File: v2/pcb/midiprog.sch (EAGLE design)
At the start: 56 parts, among them IC1 PIC18F4550_40, IC2 TPIC6B596N, IC4 TPIC6B596N, Q2 2N2222A, Q3 2N2222A, Q4 2N2222A, Q5 8MHz

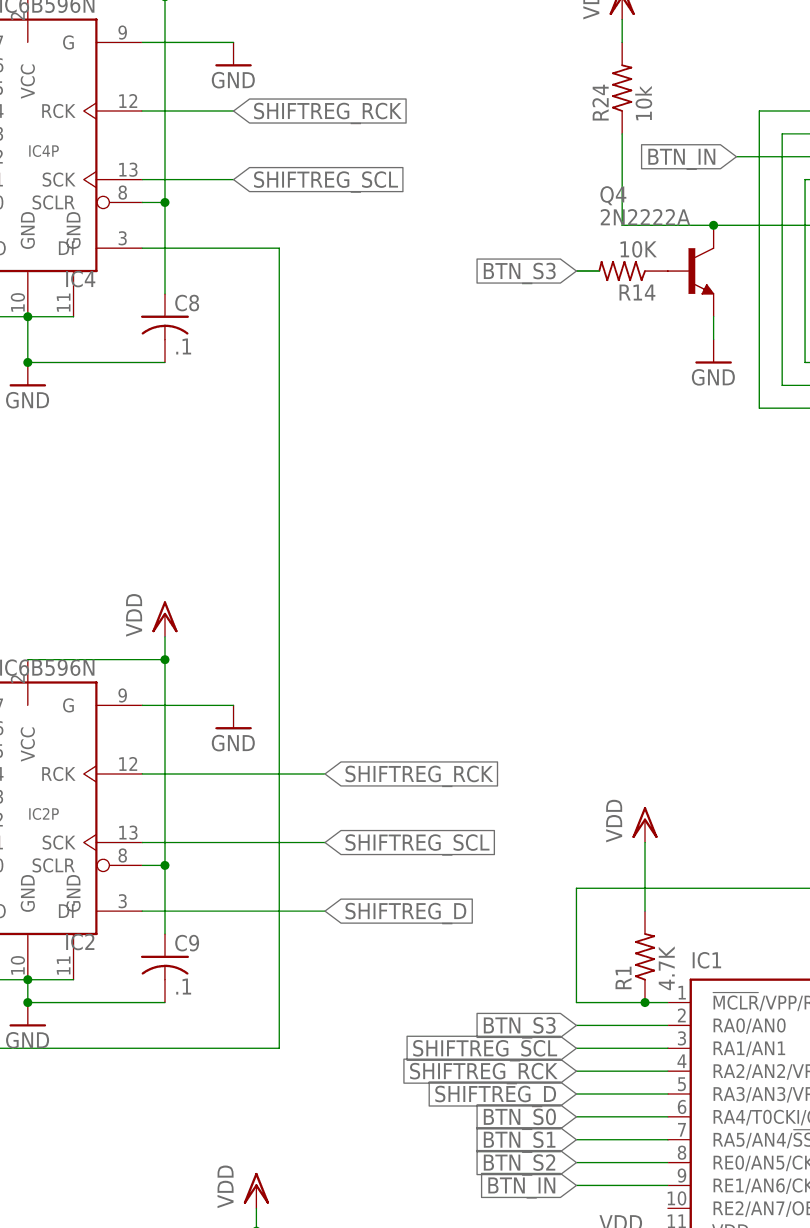
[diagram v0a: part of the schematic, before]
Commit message: Named connections better on schematic.
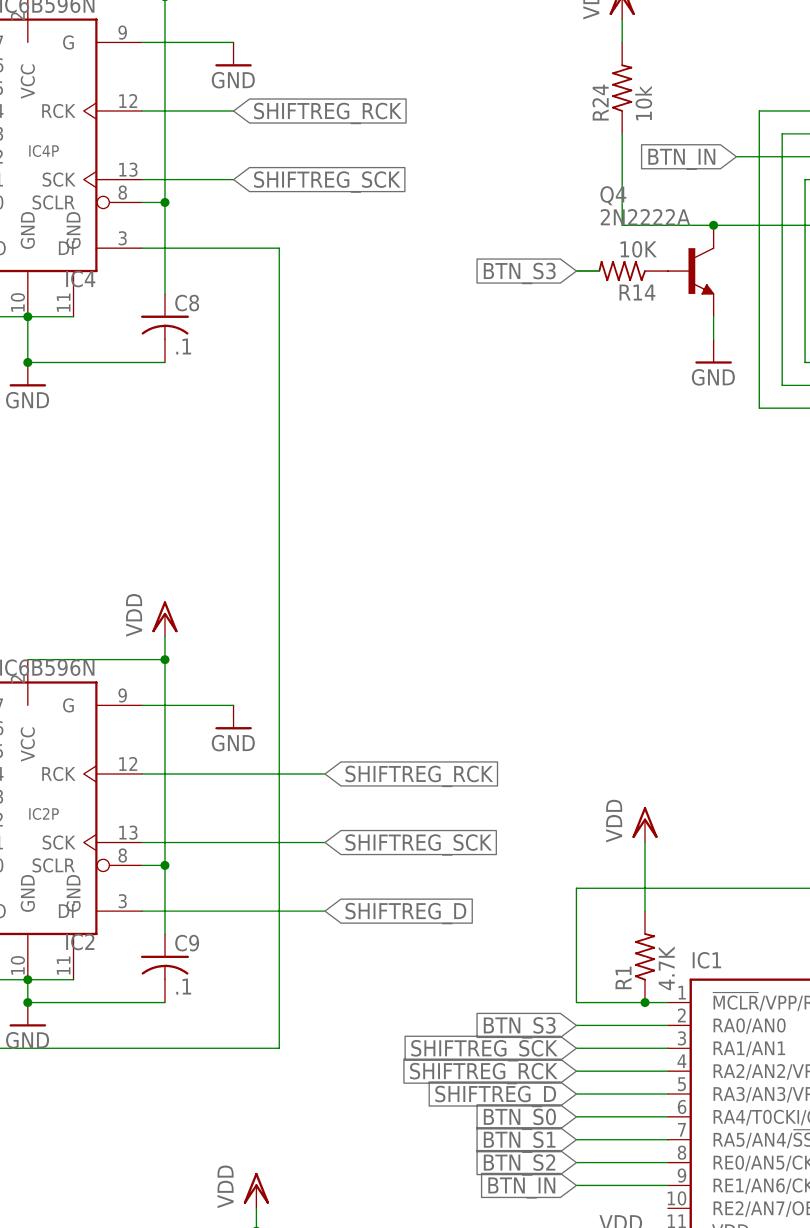
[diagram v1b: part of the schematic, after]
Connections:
- net N$46 renamed BTN_TOP_6
- net N$47 renamed BTN_BOT_6
- net N$48 renamed BTN_TOP_8
- net N$49 renamed BTN_TOP_7
- net N$50 renamed BTN_BOT_8
- net N$51 renamed BTN_BOT_7
- net N$52 renamed BTN_BOT_5
- net N$55 renamed BTN_BOT_4
- net N$56 renamed BTN_BOT_1
- net N$57 renamed BTN_BOT_2
- net N$58 renamed BTN_BOT_3
- net N$60 renamed BTN_TOP_5
- net N$61 renamed BTN_TOP_4
- net N$62 renamed BTN_TOP_1
- net N$63 renamed BTN_TOP_2
- net N$64 renamed BTN_TOP_3
- net SHIFTREG_SCL renamed SHIFTREG_SCK
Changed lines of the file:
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@@
 </segment>
 </net>
-<net name="SHIFTREG_SCL" class="0">
+<net name="SHIFTREG_SCK" class="0">
 <segment>
 <wire x1="193.04" y1="60.96" x2="213.36" y2="60.96" width="0.1524" layer="91"/>
@@
 </segment>
 </net>
-<net name="N$46" class="0">
+<net name="BTN_TOP_6" class="0">
 <segment>
 <pinref part="U$2" gate="G$1" pin="A5"/>
@@
 </segment>
 </net>
-<net name="N$48" class="0">
+<net name="BTN_TOP_8" class="0">
 <segment>
 <pinref part="U$2" gate="G$1" pin="A7"/>
@@
 </segment>
 </net>
-<net name="N$49" class="0">
+<net name="BTN_TOP_7" class="0">
 <segment>
 <pinref part="BTN_FX_CN" gate="G$1" pin="13"/>
@@
 </segment>
 </net>
-<net name="N$60" class="0">
+<net name="BTN_TOP_5" class="0">
 <segment>
 <pinref part="BTN_FX_CN" gate="G$1" pin="15"/>
@@
 </segment>
 </net>
-<net name="N$61" class="0">
+<net name="BTN_TOP_4" class="0">
 <segment>
 <pinref part="BTN_FX_CN" gate="G$1" pin="7"/>
@@
 </segment>
 </net>
-<net name="N$62" class="0">
+<net name="BTN_TOP_1" class="0">
 <segment>
 <pinref part="BTN_FX_CN" gate="G$1" pin="5"/>
@@
 </segment>
 </net>
-<net name="N$63" class="0">
+<net name="BTN_TOP_2" class="0">
 <segment>
 <pinref part="BTN_FX_CN" gate="G$1" pin="3"/>
@@
 </segment>
 </net>
-<net name="N$64" class="0">
+<net name="BTN_TOP_3" class="0">
 <segment>
 <pinref part="BTN_FX_CN" gate="G$1" pin="1"/>
@@
 </segment>
 </net>
-<net name="N$47" class="0">
+<net name="BTN_BOT_6" class="0">
 <segment>
 <pinref part="BTN_PR_CN" gate="G$1" pin="9"/>
@@
 </segment>
 </net>
-<net name="N$50" class="0">
+<net name="BTN_BOT_8" class="0">
 <segment>
 <pinref part="BTN_PR_CN" gate="G$1" pin="11"/>
@@
 </segment>
 </net>
-<net name="N$51" class="0">
+<net name="BTN_BOT_7" class="0">
 <segment>
 <pinref part="BTN_PR_CN" gate="G$1" pin="13"/>
@@
 </segment>
 </net>
-<net name="N$52" class="0">
+<net name="BTN_BOT_5" class="0">
 <segment>
 <pinref part="BTN_PR_CN" gate="G$1" pin="15"/>
@@
 </segment>
 </net>
-<net name="N$55" class="0">
+<net name="BTN_BOT_4" class="0">
 <segment>
 <pinref part="BTN_PR_CN" gate="G$1" pin="7"/>
@@
 </segment>
 </net>
-<net name="N$56" class="0">
+<net name="BTN_BOT_1" class="0">
 <segment>
 <pinref part="BTN_PR_CN" gate="G$1" pin="5"/>
@@
 </segment>
 </net>
-<net name="N$57" class="0">
+<net name="BTN_BOT_2" class="0">
 <segment>
 <pinref part="BTN_PR_CN" gate="G$1" pin="3"/>
@@
 </segment>
 </net>
-<net name="N$58" class="0">
+<net name="BTN_BOT_3" class="0">
 <segment>
 <pinref part="BTN_PR_CN" gate="G$1" pin="1"/>

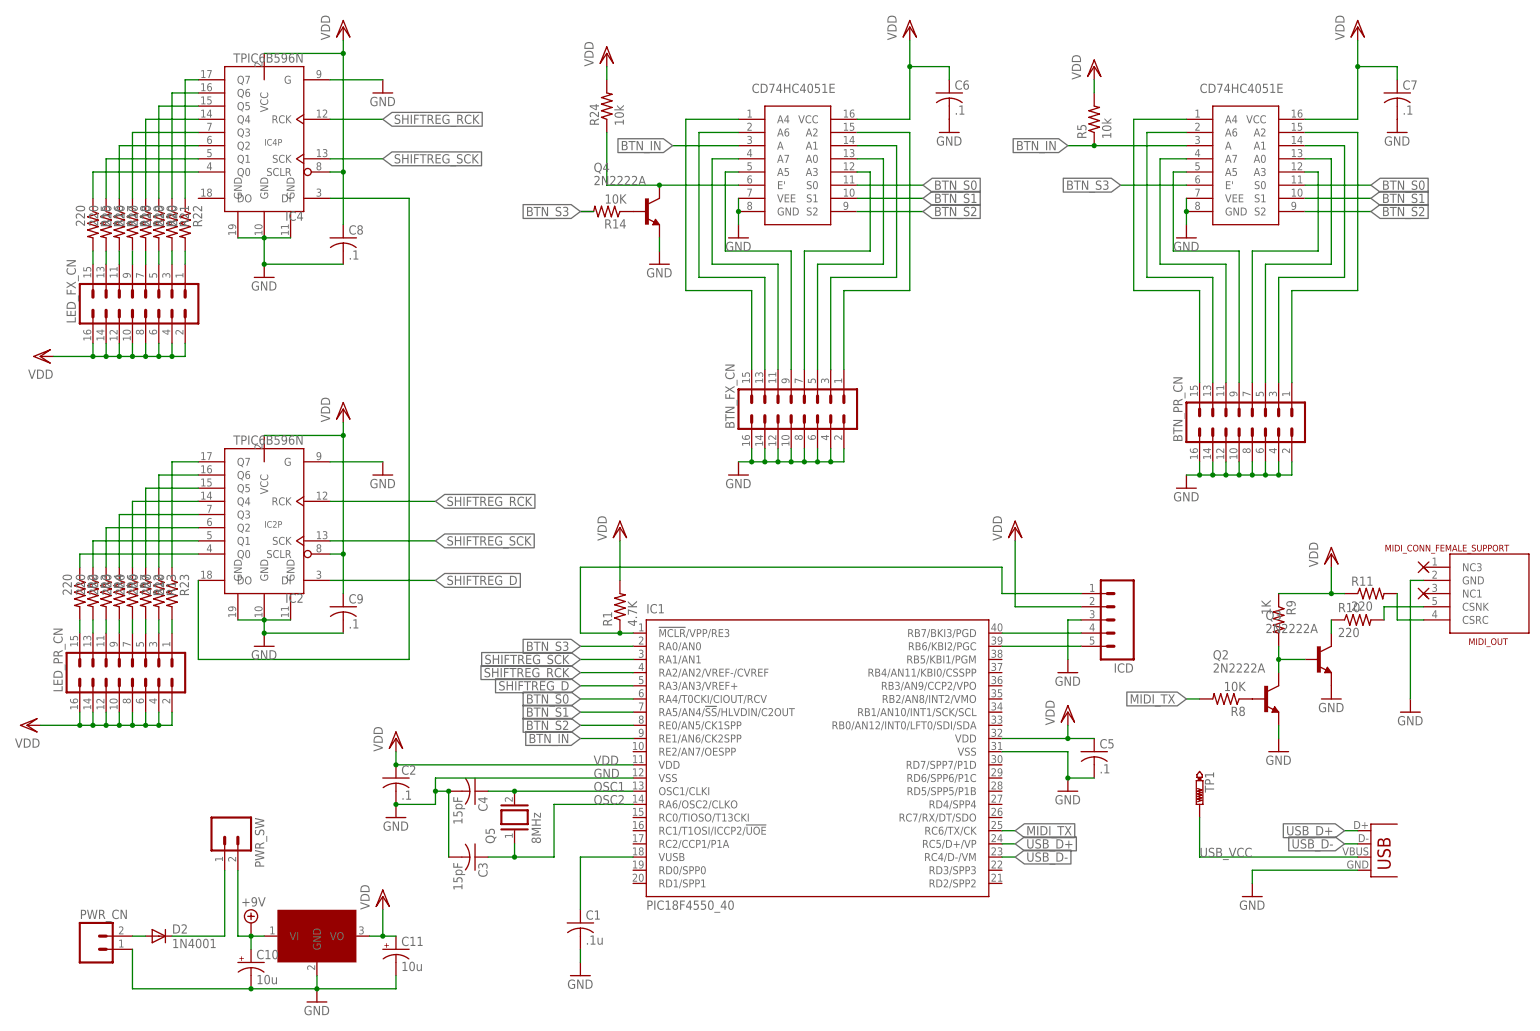
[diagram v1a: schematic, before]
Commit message: Renamed pins and connectors on schematic and added proper labels.
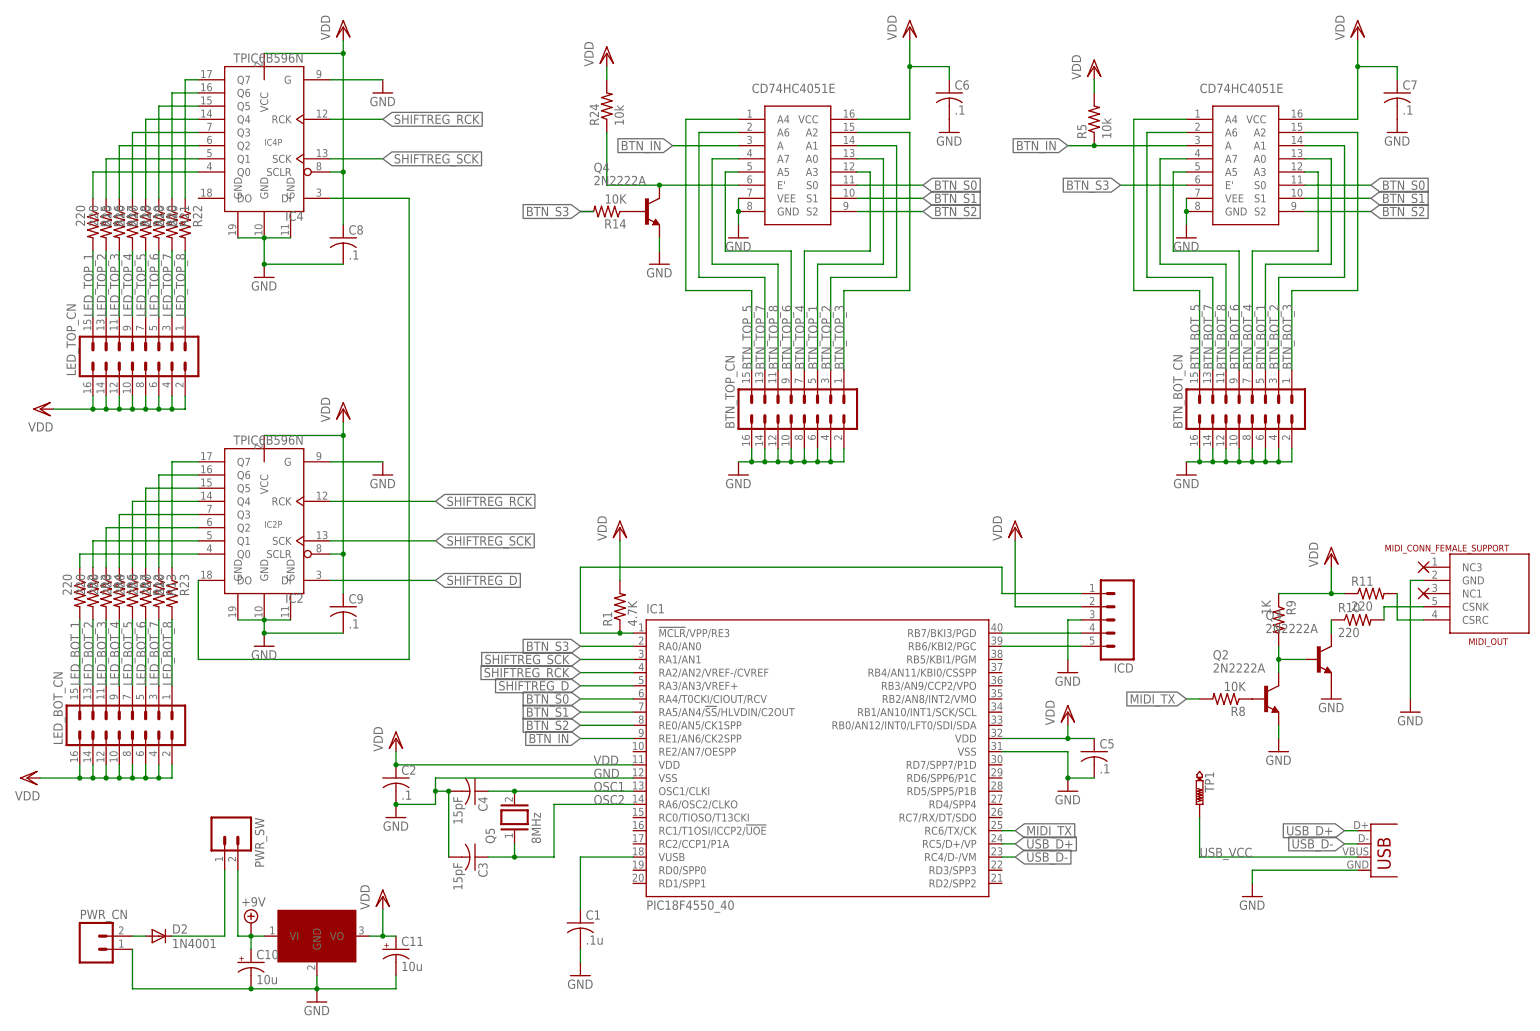
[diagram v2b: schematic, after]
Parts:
- removed BTN_PR_CN, LED_FX_CN, LED_PR_CN: (no value), con-lstb:MA08-2
- added BTN_BOT_CN, LED_BOT_CN, LED_TOP_CN: (no value), con-lstb:MA08-2
- renumbered BTN_FX_CN to BTN_TOP_CN
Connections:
- removed net N$10: LED_FX_CN.11, R17.2
- removed net N$11: LED_FX_CN.9, R18.2
- removed net N$12: LED_FX_CN.7, R19.2
- removed net N$13: LED_FX_CN.5, R20.2
- removed net N$14: LED_FX_CN.3, R21.2
- removed net N$15: LED_FX_CN.1, R22.2
- removed net N$2: LED_FX_CN.15, R15.2
- removed net N$24: LED_PR_CN.13, R3.2
- removed net N$27: LED_PR_CN.11, R4.2
- removed net N$28: LED_PR_CN.9, R6.2
- removed net N$3: LED_FX_CN.13, R16.2
- removed net N$30: LED_PR_CN.7, R7.2
- removed net N$32: LED_PR_CN.5, R12.2
- removed net N$36: LED_PR_CN.3, R13.2
- removed net N$37: LED_PR_CN.1, R23.2
- removed net N$6: LED_PR_CN.15, R2.2
- new net LED_BOT_1: LED_BOT_CN.15, R2.2
- new net LED_BOT_2: LED_BOT_CN.13, R3.2
- new net LED_BOT_3: LED_BOT_CN.11, R4.2
- new net LED_BOT_4: LED_BOT_CN.9, R6.2
- new net LED_BOT_5: LED_BOT_CN.7, R7.2
- new net LED_BOT_6: LED_BOT_CN.5, R12.2
- new net LED_BOT_7: LED_BOT_CN.3, R13.2
- new net LED_BOT_8: LED_BOT_CN.1, R23.2
- new net LED_TOP_1: LED_TOP_CN.15, R15.2
- new net LED_TOP_2: LED_TOP_CN.13, R16.2
- new net LED_TOP_3: LED_TOP_CN.11, R17.2
- new net LED_TOP_4: LED_TOP_CN.9, R18.2
- new net LED_TOP_5: LED_TOP_CN.7, R19.2
- new net LED_TOP_6: LED_TOP_CN.5, R20.2
- new net LED_TOP_7: LED_TOP_CN.3, R21.2
- new net LED_TOP_8: LED_TOP_CN.1, R22.2
- net BTN_BOT_1: now also BTN_BOT_CN.5; no longer BTN_PR_CN.5
- net BTN_BOT_2: now also BTN_BOT_CN.3; no longer BTN_PR_CN.3
- net BTN_BOT_3: now also BTN_BOT_CN.1; no longer BTN_PR_CN.1
- net BTN_BOT_4: now also BTN_BOT_CN.7; no longer BTN_PR_CN.7
- net BTN_BOT_5: now also BTN_BOT_CN.15; no longer BTN_PR_CN.15
- net BTN_BOT_6: now also BTN_BOT_CN.9; no longer BTN_PR_CN.9
- net BTN_BOT_7: now also BTN_BOT_CN.13; no longer BTN_PR_CN.13
- net BTN_BOT_8: now also BTN_BOT_CN.11; no longer BTN_PR_CN.11
- net GND: now also BTN_BOT_CN.10, BTN_BOT_CN.12, BTN_BOT_CN.14, BTN_BOT_CN.16, BTN_BOT_CN.2, BTN_BOT_CN.4, BTN_BOT_CN.6, BTN_BOT_CN.8; no longer BTN_PR_CN.10, BTN_PR_CN.12, BTN_PR_CN.14, BTN_PR_CN.16, BTN_PR_CN.2, BTN_PR_CN.4, BTN_PR_CN.6, BTN_PR_CN.8
- net VDD: now also LED_BOT_CN.10, LED_BOT_CN.12, LED_BOT_CN.14, LED_BOT_CN.16, LED_BOT_CN.2, LED_BOT_CN.4, LED_BOT_CN.6, LED_BOT_CN.8, LED_TOP_CN.10, LED_TOP_CN.12, LED_TOP_CN.14, LED_TOP_CN.16, LED_TOP_CN.2, LED_TOP_CN.4, LED_TOP_CN.6, LED_TOP_CN.8; no longer LED_FX_CN.10, LED_FX_CN.12, LED_FX_CN.14, LED_FX_CN.16, LED_FX_CN.2, LED_FX_CN.4, LED_FX_CN.6, LED_FX_CN.8, LED_PR_CN.10, LED_PR_CN.12, LED_PR_CN.14, LED_PR_CN.16, LED_PR_CN.2, LED_PR_CN.4, LED_PR_CN.6, LED_PR_CN.8
